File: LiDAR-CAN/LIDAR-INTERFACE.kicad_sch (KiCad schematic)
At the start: 31 parts, among them U3 W5500, Y1 25MHz

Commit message: Update complete first placement
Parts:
- removed TP20: TestPoint, TestPoint:TestPoint_Pad_D1.0mm, symbol Connector:TestPoint
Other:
- moved on the sheet: TP17, TP18, TP19
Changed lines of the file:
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@@
 	(text_box "Testpoints"
 		(exclude_from_sim no)
-		(at 196.85 139.7 0)
-		(size 82.55 19.05)
+		(at 203.2 139.7 0)
+		(size 76.2 19.05)
 		(margins 0.9525 0.9525 0.9525 0.9525)
 		(stroke
@@
 	(wire
 		(pts
-			(xy 215.9 148.59) (xy 215.9 151.13)
+			(xy 228.6 148.59) (xy 228.6 151.13)
 		)
 		(stroke
@@
 	(wire
 		(pts
-			(xy 241.3 148.59) (xy 241.3 151.13)
-		)
-		(stroke
-			(width 0)
-			(type default)
-		)
-	)
-	(wire
-		(pts
 			(xy 76.2 50.8) (xy 76.2 53.34)
 		)
@@
 	(wire
 		(pts
-			(xy 228.6 148.59) (xy 228.6 151.13)
+			(xy 241.3 148.59) (xy 241.3 151.13)
 		)
 		(stroke
@@
 	(wire
 		(pts
-			(xy 203.2 148.59) (xy 203.2 151.13)
+			(xy 215.9 148.59) (xy 215.9 151.13)
 		)
 		(stroke
@@
 	)
 	(label "1V20"
-		(at 228.6 151.13 270)
+		(at 241.3 151.13 270)
 		(effects
 			(font
@@
 	)
 	(label "AVDD"
-		(at 215.9 151.13 270)
+		(at 228.6 151.13 270)
 		(effects
 			(font
@@
 	(hierarchical_label "~{SCS}"
 		(shape input)
-		(at 241.3 151.13 270)
-		(effects
-			(font
-				(size 1.27 1.27)
-			)
-			(justify right)
-		)
-	)
-	(hierarchical_label "~{SCS}"
-		(shape input)
 		(at 114.3 91.44 180)
 		(effects
@@
 	(hierarchical_label "VDD"
 		(shape input)
-		(at 203.2 151.13 270)
+		(at 215.9 151.13 270)
 		(effects
 			(font
@@
 	)
 	(symbol
-		(lib_id "Connector:TestPoint")
-		(at 241.3 148.59 0)
-		(unit 1)
-		(exclude_from_sim no)
-		(in_bom no)
-		(on_board yes)
-		(dnp no)
-		(fields_autoplaced yes)
-		(property "Reference" "TP20"
-			(at 243.84 144.0179 0)
-			(effects
-				(font
-					(size 1.27 1.27)
-				)
-				(justify left)
-			)
-		)
-		(property "Value" "TestPoint"
-			(at 243.84 146.5579 0)
-			(effects
-				(font
-					(size 1.27 1.27)
-				)
-				(justify left)
-			)
-		)
-		(property "Footprint" "TestPoint:TestPoint_Pad_D1.0mm"
-			(at 246.38 148.59 0)
-			(effects
-				(font
-					(size 1.27 1.27)
-				)
-				(hide yes)
-			)
-		)
-		(property "Datasheet" "~"
-			(at 246.38 148.59 0)
-			(effects
-				(font
-					(size 1.27 1.27)
-				)
-				(hide yes)
-			)
-		)
-		(property "Description" "test point"
-			(at 241.3 148.59 0)
-			(effects
-				(font
-					(size 1.27 1.27)
-				)
-				(hide yes)
-			)
-		)
-		(pin "1"
-		)
-		(instances
-			(project "LiDAR-CAN"
-				(path "/56db6f21-0e4a-4321-bd8a-db37f1842dd9/91fe436f-7e8c-47e0-899c-e39330e04729"
-					(reference "TP20")
-					(unit 1)
-				)
-			)
-		)
-	)
-	(symbol
 		(lib_id "Symbols:CAP CER 0.1UF 50V X7R 0603")
 		(at 127 57.15 180)
@@
 	(symbol
 		(lib_id "Connector:TestPoint")
-		(at 228.6 148.59 0)
+		(at 241.3 148.59 0)
 		(unit 1)
 		(exclude_from_sim no)
@@
 		(fields_autoplaced yes)
 		(property "Reference" "TP19"
-			(at 231.14 144.0179 0)
+			(at 243.84 144.0179 0)
 			(effects
 				(font
@@
 		)
 		(property "Value" "TestPoint"
-			(at 231.14 146.5579 0)
+			(at 243.84 146.5579 0)
 			(effects
 				(font
@@
 		)
 		(property "Footprint" "TestPoint:TestPoint_Pad_D1.0mm"
-			(at 233.68 148.59 0)
+			(at 246.38 148.59 0)
 			(effects
 				(font
@@
 		)
 		(property "Datasheet" "~"
-			(at 233.68 148.59 0)
+			(at 246.38 148.59 0)
 			(effects
 				(font
@@
 		)
 		(property "Description" "test point"
-			(at 228.6 148.59 0)
+			(at 241.3 148.59 0)
 			(effects
 				(font
@@
 	(symbol
 		(lib_id "Connector:TestPoint")
-		(at 203.2 148.59 0)
+		(at 215.9 148.59 0)
 		(unit 1)
 		(exclude_from_sim no)
@@
 		(fields_autoplaced yes)
 		(property "Reference" "TP17"
-			(at 205.74 144.0179 0)
+			(at 218.44 144.0179 0)
 			(effects
 				(font
@@
 		)
 		(property "Value" "TestPoint"
-			(at 205.74 146.5579 0)
+			(at 218.44 146.5579 0)
 			(effects
 				(font
@@
 		)
 		(property "Footprint" "TestPoint:TestPoint_Pad_D1.0mm"
-			(at 208.28 148.59 0)
+			(at 220.98 148.59 0)
 			(effects
 				(font
@@
 		)
 		(property "Datasheet" "~"
-			(at 208.28 148.59 0)
+			(at 220.98 148.59 0)
 			(effects
 				(font
@@
 		)
 		(property "Description" "test point"
-			(at 203.2 148.59 0)
+			(at 215.9 148.59 0)
 			(effects
 				(font
@@
 	(symbol
 		(lib_id "Connector:TestPoint")
-		(at 215.9 148.59 0)
+		(at 228.6 148.59 0)
 		(unit 1)
 		(exclude_from_sim no)
@@
 		(fields_autoplaced yes)
 		(property "Reference" "TP18"
-			(at 218.44 144.0179 0)
+			(at 231.14 144.0179 0)
 			(effects
 				(font
@@
 		)
 		(property "Value" "TestPoint"
-			(at 218.44 146.5579 0)
+			(at 231.14 146.5579 0)
 			(effects
 				(font
@@
 		)
 		(property "Footprint" "TestPoint:TestPoint_Pad_D1.0mm"
-			(at 220.98 148.59 0)
+			(at 233.68 148.59 0)
 			(effects
 				(font
@@
 		)
 		(property "Datasheet" "~"
-			(at 220.98 148.59 0)
+			(at 233.68 148.59 0)
 			(effects
 				(font
@@
 		)
 		(property "Description" "test point"
-			(at 215.9 148.59 0)
+			(at 228.6 148.59 0)
 			(effects
 				(font

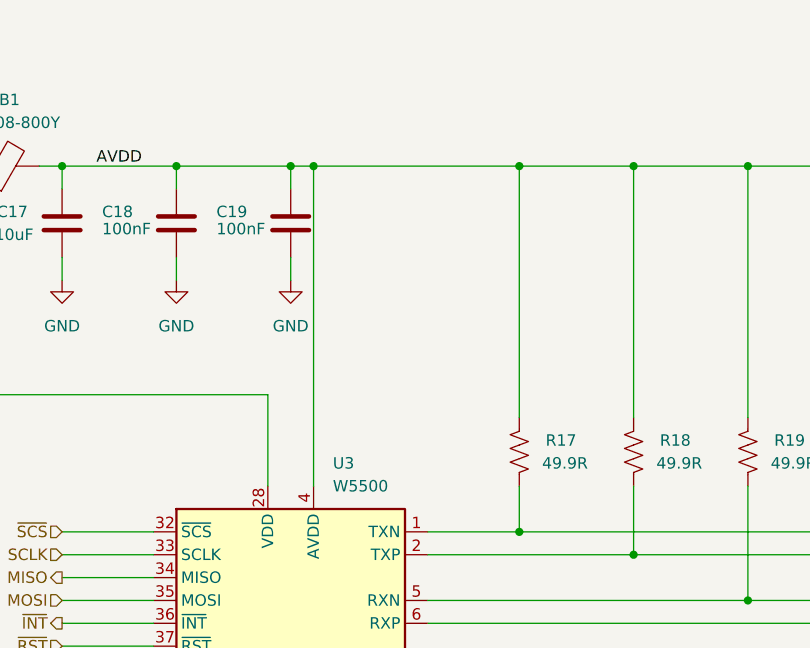
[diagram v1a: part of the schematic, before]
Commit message: Add Ethernet interface routing
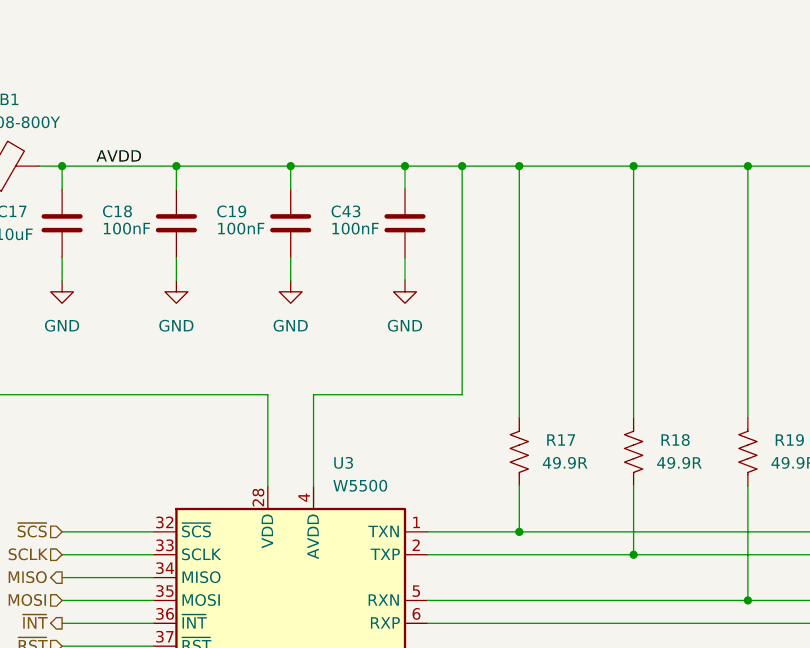
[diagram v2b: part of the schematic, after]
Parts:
- added C43: 100nF, Capacitor_SMD:C_0603_1608Metric, symbol Symbols:CAP CER 0.1UF 50V X7R 0603
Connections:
- net AVDD: now also C43.2
- net GND: now also C43.1
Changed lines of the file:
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@@
 	)
 	(junction
+		(at 158.75 50.8)
+		(diameter 0)
+		(color 0 0 0 0)
+	)
+	(junction
 		(at 88.9 50.8)
 		(diameter 0)
@@
 	)
 	(junction
+		(at 152.4 50.8)
+		(diameter 0)
+		(color 0 0 0 0)
+	)
+	(junction
 		(at 177.8 50.8)
 		(diameter 0)
@@
 	)
 	(junction
-		(at 142.24 50.8)
-		(diameter 0)
-		(color 0 0 0 0)
-	)
-	(junction
 		(at 190.5 99.06)
 		(diameter 0)
@@
 	(wire
 		(pts
+			(xy 142.24 76.2) (xy 142.24 86.36)
+		)
+		(stroke
+			(width 0)
+			(type default)
+		)
+	)
+	(wire
+		(pts
 			(xy 101.6 76.2) (xy 101.6 50.8)
 		)
@@
 	(wire
 		(pts
+			(xy 152.4 60.96) (xy 152.4 63.5)
+		)
+		(stroke
+			(width 0)
+			(type default)
+		)
+	)
+	(wire
+		(pts
 			(xy 154.94 124.46) (xy 190.5 124.46)
 		)
@@
 	(wire
 		(pts
+			(xy 152.4 50.8) (xy 158.75 50.8)
+		)
+		(stroke
+			(width 0)
+			(type default)
+		)
+	)
+	(wire
+		(pts
 			(xy 165.1 91.44) (xy 215.9 91.44)
 		)
@@
 	(wire
 		(pts
+			(xy 158.75 76.2) (xy 142.24 76.2)
+		)
+		(stroke
+			(width 0)
+			(type default)
+		)
+	)
+	(wire
+		(pts
 			(xy 190.5 50.8) (xy 190.5 78.74)
 		)
@@
 	(wire
 		(pts
-			(xy 88.9 127) (xy 88.9 130.81)
+			(xy 152.4 50.8) (xy 152.4 53.34)
 		)
 		(stroke
@@
 	(wire
 		(pts
-			(xy 254 104.14) (xy 254 100.33)
+			(xy 88.9 127) (xy 88.9 130.81)
 		)
 		(stroke
@@
 	(wire
 		(pts
-			(xy 114.3 91.44) (xy 124.46 91.44)
+			(xy 254 104.14) (xy 254 100.33)
 		)
 		(stroke
@@
 	(wire
 		(pts
-			(xy 76.2 50.8) (xy 88.9 50.8)
+			(xy 114.3 91.44) (xy 124.46 91.44)
 		)
 		(stroke
@@
 	(wire
 		(pts
-			(xy 241.3 92.71) (xy 241.3 104.14)
+			(xy 76.2 50.8) (xy 88.9 50.8)
 		)
 		(stroke
@@
 	(wire
 		(pts
-			(xy 241.3 111.76) (xy 241.3 114.3)
+			(xy 241.3 92.71) (xy 241.3 104.14)
 		)
 		(stroke
@@
 	(wire
 		(pts
-			(xy 142.24 50.8) (xy 165.1 50.8)
+			(xy 241.3 111.76) (xy 241.3 114.3)
 		)
 		(stroke
@@
 	(wire
 		(pts
-			(xy 142.24 50.8) (xy 139.7 50.8)
+			(xy 139.7 50.8) (xy 152.4 50.8)
 		)
 		(stroke
@@
 	(wire
 		(pts
+			(xy 158.75 50.8) (xy 165.1 50.8)
+		)
+		(stroke
+			(width 0)
+			(type default)
+		)
+	)
+	(wire
+		(pts
 			(xy 165.1 50.8) (xy 165.1 78.74)
 		)
@@
 	(wire
 		(pts
-			(xy 142.24 50.8) (xy 142.24 86.36)
+			(xy 158.75 50.8) (xy 158.75 76.2)
 		)
 		(stroke
@@
 	)
 	(symbol
+		(lib_id "Symbols:CAP CER 0.1UF 50V X7R 0603")
+		(at 152.4 57.15 180)
+		(unit 1)
+		(exclude_from_sim no)
+		(in_bom yes)
+		(on_board yes)
+		(dnp no)
+		(property "Reference" "C43"
+			(at 144.145 55.88 0)
+			(effects
+				(font
+					(size 1.27 1.27)
+				)
+				(justify right)
+			)
+		)
+		(property "Value" "100nF"
+			(at 144.145 57.785 0)
+			(effects
+				(font
+					(size 1.27 1.27)
+				)
+				(justify right)
+			)
+		)
+		(property "Footprint" "Capacitor_SMD:C_0603_1608Metric"
+			(at 151.13 45.72 0)
+			(effects
+				(font
+					(size 1.27 1.27)
+				)
+				(hide yes)
+			)
+		)
+		(property "Datasheet" "https://datasheets.kyocera-avx.com/KGM_X7R.pdf"
+			(at 152.4 48.26 0)
+			(effects
+				(font
+					(size 1.27 1.27)
+				)
+				(hide yes)
+			)
+		)
+		(property "Description" "CAP CER 0.1UF 50V X7R 0603"
+			(at 152.4 57.15 0)
+			(effects
+				(font
+					(size 1.27 1.27)
+				)
+				(hide yes)
+			)
+		)
+		(property "Vendor" "KYOCERA AVX"
+			(at 152.4 43.18 0)
+			(effects
+				(font
+					(size 1.27 1.27)
+				)
+				(hide yes)
+			)
+		)
+		(property "MPN" "KGM15BR71H104KM"
+			(at 152.4 50.8 0)
+			(effects
+				(font
+					(size 1.27 1.27)
+				)
+				(hide yes)
+			)
+		)
+		(property "Manufacturer" "KYOCERA AVX"
+			(at 152.4 57.15 0)
+			(effects
+				(font
+					(size 1.27 1.27)
+				)
+				(hide yes)
+			)
+		)
+		(pin "1"
+		)
+		(pin "2"
+		)
+		(instances
+			(project "LiDAR-CAN"
+				(path "/56db6f21-0e4a-4321-bd8a-db37f1842dd9/91fe436f-7e8c-47e0-899c-e39330e04729"
+					(reference "C43")
+					(unit 1)
+				)
+			)
+		)
+	)
+	(symbol
 		(lib_id "Connector:TestPoint")
 		(at 266.7 148.59 0)
@@
 					(unit 1)
 				)
+			)
+		)
+	)
+	(symbol
+		(lib_id "power:GND")
+		(at 152.4 63.5 0)
+		(unit 1)
+		(exclude_from_sim no)
+		(in_bom yes)
+		(on_board yes)
+		(dnp no)
+		(property "Reference" "#PWR079"
+			(at 152.4 69.85 0)
+			(effects
+				(font
+					(size 1.27 1.27)
+				)
+				(hide yes)
+			)
+		)
+		(property "Value" "GND"
+			(at 152.4 68.58 0)
+			(effects
+				(font
+					(size 1.27 1.27)
+				)
+			)
+		)
+		(property "Footprint" ""
+			(at 152.4 63.5 0)
+			(effects
+				(font
+					(size 1.27 1.27)
+				)
+				(hide yes)
+			)
+		)
+		(property "Datasheet" ""
+			(at 152.4 63.5 0)
+			(effects
+				(font
+					(size 1.27 1.27)
+				)
+				(hide yes)
+			)
+		)
+		(property "Description" "Power symbol creates a global label with name \"GND\" , ground"
+			(at 152.4 63.5 0)
+			(effects
+				(font
+					(size 1.27 1.27)
+				)
+				(hide yes)
+			)
+		)
+		(pin "1"
+		)
+		(instances
+			(project "LiDAR-CAN"
+				(path "/56db6f21-0e4a-4321-bd8a-db37f1842dd9/91fe436f-7e8c-47e0-899c-e39330e04729"
+					(reference "#PWR079")
+					(unit 1)
+				)
